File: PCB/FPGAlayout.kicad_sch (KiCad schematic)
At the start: 6 parts, among them U3 XC7A100T-FTG256

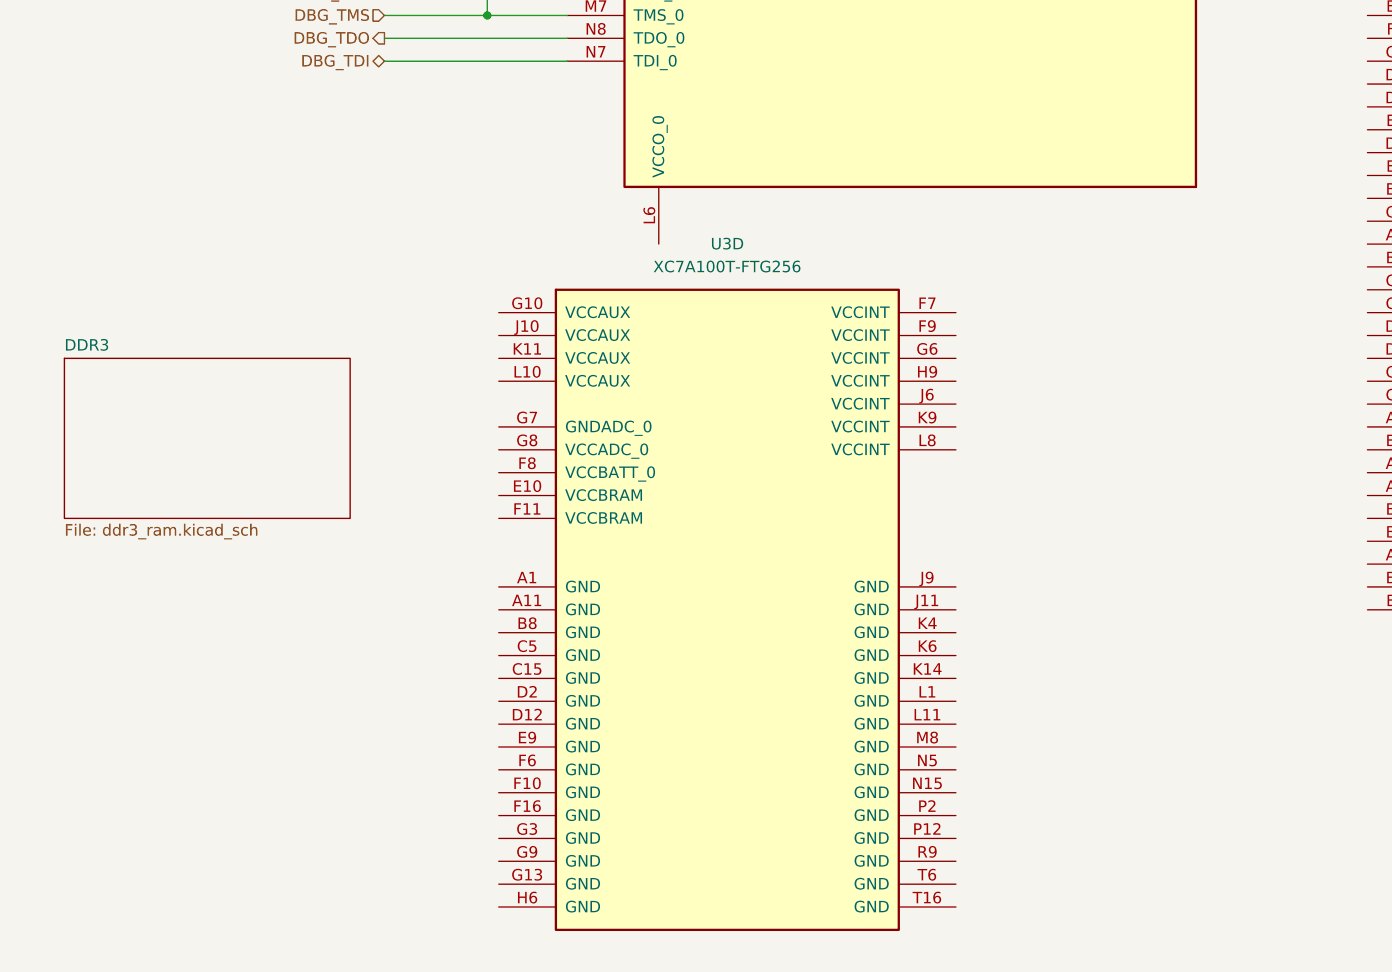
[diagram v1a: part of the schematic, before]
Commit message: Trace QSPI for MCU Master (#7), slaves unconnected
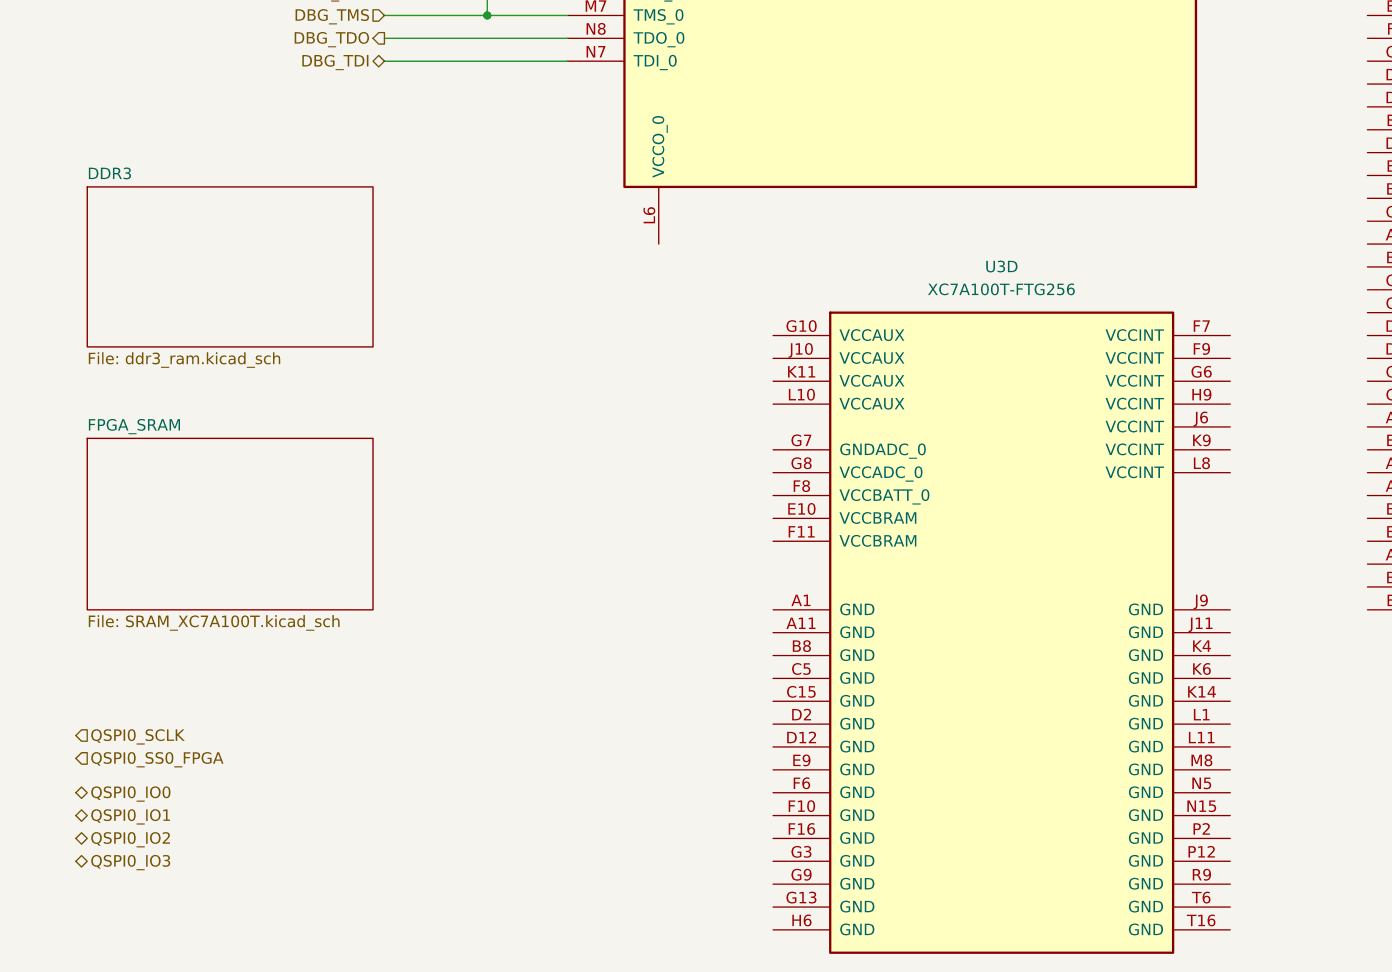
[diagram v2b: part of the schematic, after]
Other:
- added sheet FPGA_SRAM (SRAM_XC7A100T.kicad_sch)
- moved on the sheet: U3D
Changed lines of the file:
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@@
     (stroke (width 0) (type default))
+  )
+  (hierarchical_label "QSPI0_IO1" (shape bidirectional) (at 22.86 170.18 0) (fields_autoplaced)
+    (effects (font (size 1.27 1.27)) (justify left))
+  )
+  (hierarchical_label "QSPI0_SS0_FPGA" (shape input) (at 22.86 163.83 0) (fields_autoplaced)
+    (effects (font (size 1.27 1.27)) (justify left))
   )
   (hierarchical_label "PROGRAM_B_0" (shape output) (at 62.23 55.88 180) (fields_autoplaced)
@@
     (effects (font (size 1.27 1.27)) (justify right))
   )
+  (hierarchical_label "QSPI0_SCLK" (shape input) (at 22.86 161.29 0) (fields_autoplaced)
+    (effects (font (size 1.27 1.27)) (justify left))
+  )
+  (hierarchical_label "QSPI0_IO2" (shape bidirectional) (at 22.86 172.72 0) (fields_autoplaced)
+    (effects (font (size 1.27 1.27)) (justify left))
+  )
   (hierarchical_label "DBG_TMS" (shape input) (at 57.15 81.28 180) (fields_autoplaced)
     (effects (font (size 1.27 1.27)) (justify right))
   )
+  (hierarchical_label "QSPI0_IO0" (shape bidirectional) (at 22.86 167.64 0) (fields_autoplaced)
+    (effects (font (size 1.27 1.27)) (justify left))
+  )
   (hierarchical_label "DBG_TCK" (shape input) (at 57.15 78.74 180) (fields_autoplaced)
     (effects (font (size 1.27 1.27)) (justify right))
@@
   (hierarchical_label "DBG_TDI" (shape bidirectional) (at 57.15 86.36 180) (fields_autoplaced)
     (effects (font (size 1.27 1.27)) (justify right))
+  )
+  (hierarchical_label "QSPI0_IO3" (shape bidirectional) (at 22.86 175.26 0) (fields_autoplaced)
+    (effects (font (size 1.27 1.27)) (justify left))
   )
   (hierarchical_label "DBG_TDO" (shape output) (at 57.15 83.82 180) (fields_autoplaced)
@@
     )
   )
-  (symbol (lib_id "FPGA_Xilinx_Artix7:XC7A100T-FTG256") (at 95.25 147.32 0) (unit 4)
+  (symbol (lib_id "FPGA_Xilinx_Artix7:XC7A100T-FTG256") (at 125.73 149.86 0) (unit 4)
     (in_bom yes) (on_board yes) (dnp no) (fields_autoplaced)
-    (property "Reference" "U3" (at 95.25 106.68 0)
+    (property "Reference" "U3" (at 125.73 109.22 0)
       (effects (font (size 1.27 1.27)))
     )
-    (property "Value" "XC7A100T-FTG256" (at 95.25 109.22 0)
+    (property "Value" "XC7A100T-FTG256" (at 125.73 111.76 0)
       (effects (font (size 1.27 1.27)))
     )
-    (property "Footprint" "" (at 95.25 147.32 0)
-      (effects (font (size 1.27 1.27)) hide)
-    )
-    (property "Datasheet" "" (at 95.25 147.32 0)
+    (property "Footprint" "" (at 125.73 149.86 0)
+      (effects (font (size 1.27 1.27)) hide)
+    )
+    (property "Datasheet" "" (at 125.73 149.86 0)
       (effects (font (size 1.27 1.27)))
     )
@@
     )
   )
-  (sheet (at 21.59 119.38) (size 31.75 17.78) (fields_autoplaced)
+  (sheet (at 24.13 128.27) (size 31.75 19.05) (fields_autoplaced)
     (stroke (width 0.1524) (type solid))
     (fill (color 0 0 0 0.0000))
-    (property "Sheetname" "DDR3" (at 21.59 118.6684 0)
+    (property "Sheetname" "FPGA_SRAM" (at 24.13 127.5584 0)
       (effects (font (size 1.27 1.27)) (justify left bottom))
     )
-    (property "Sheetfile" "ddr3_ram.kicad_sch" (at 21.59 137.7446 0)
+    (property "Sheetfile" "SRAM_XC7A100T.kicad_sch" (at 24.13 147.9046 0)
       (effects (font (size 1.27 1.27)) (justify left top))
     )
+    (instances
+      (project "RayTracingPCB"
+        (path "/e9047d94-28be-4266-894b-6ee25ef088bd/5a7a2c0a-f09d-4b4f-9411-f51dd121457c" (page "10"))
+      )
+    )
+  )
+  (sheet (at 24.13 100.33) (size 31.75 17.78) (fields_autoplaced)
+    (stroke (width 0.1524) (type solid))
+    (fill (color 0 0 0 0.0000))
+    (property "Sheetname" "DDR3" (at 24.13 99.6184 0)
+      (effects (font (size 1.27 1.27)) (justify left bottom))
+    )
+    (property "Sheetfile" "ddr3_ram.kicad_sch" (at 24.13 118.6946 0)
+      (effects (font (size 1.27 1.27)) (justify left top))
+    )

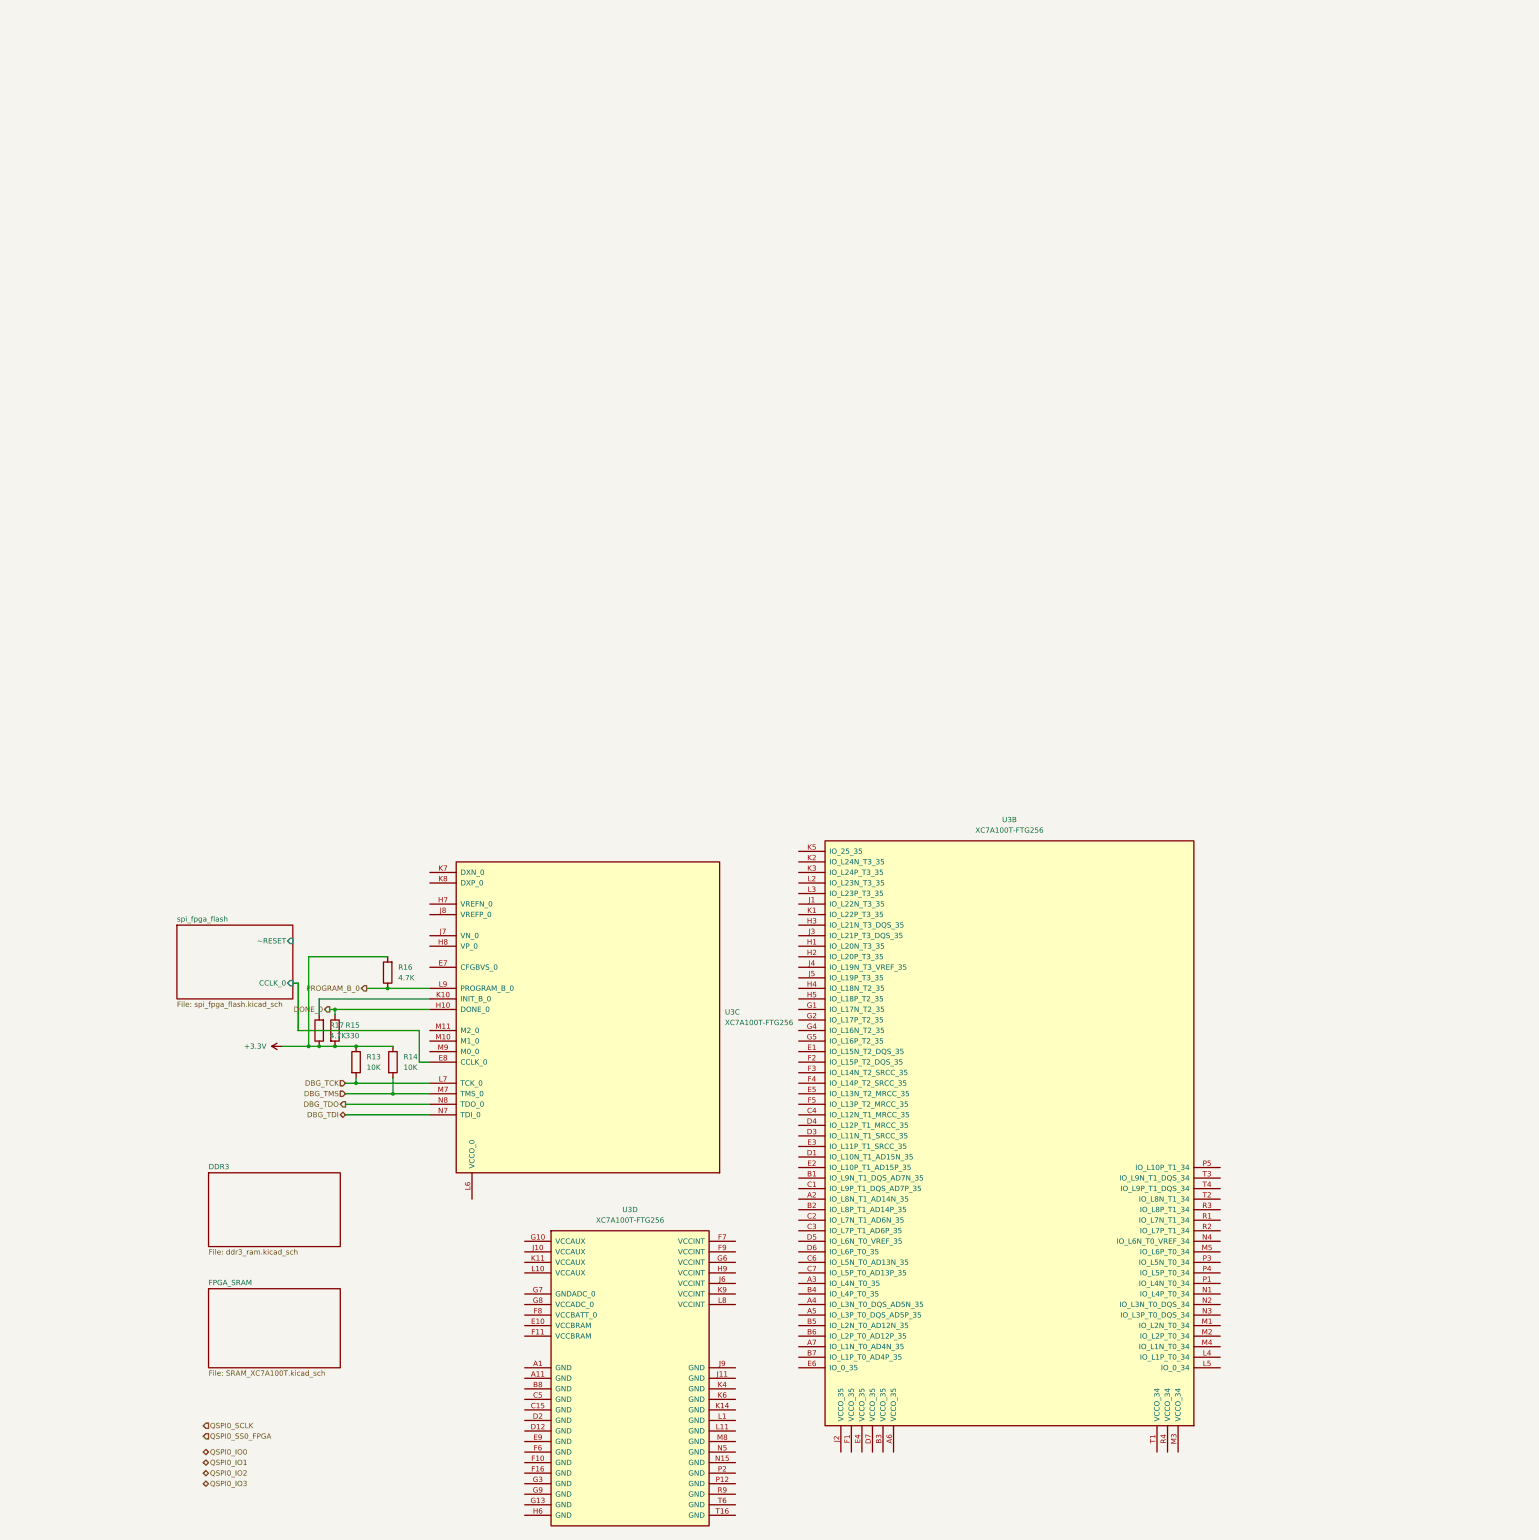
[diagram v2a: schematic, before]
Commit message: pcb: cleanup mcu sram (#10)
Co-authored-by: Kolbjørn Austreng <kolbjorn.austreng@hotzen.io>
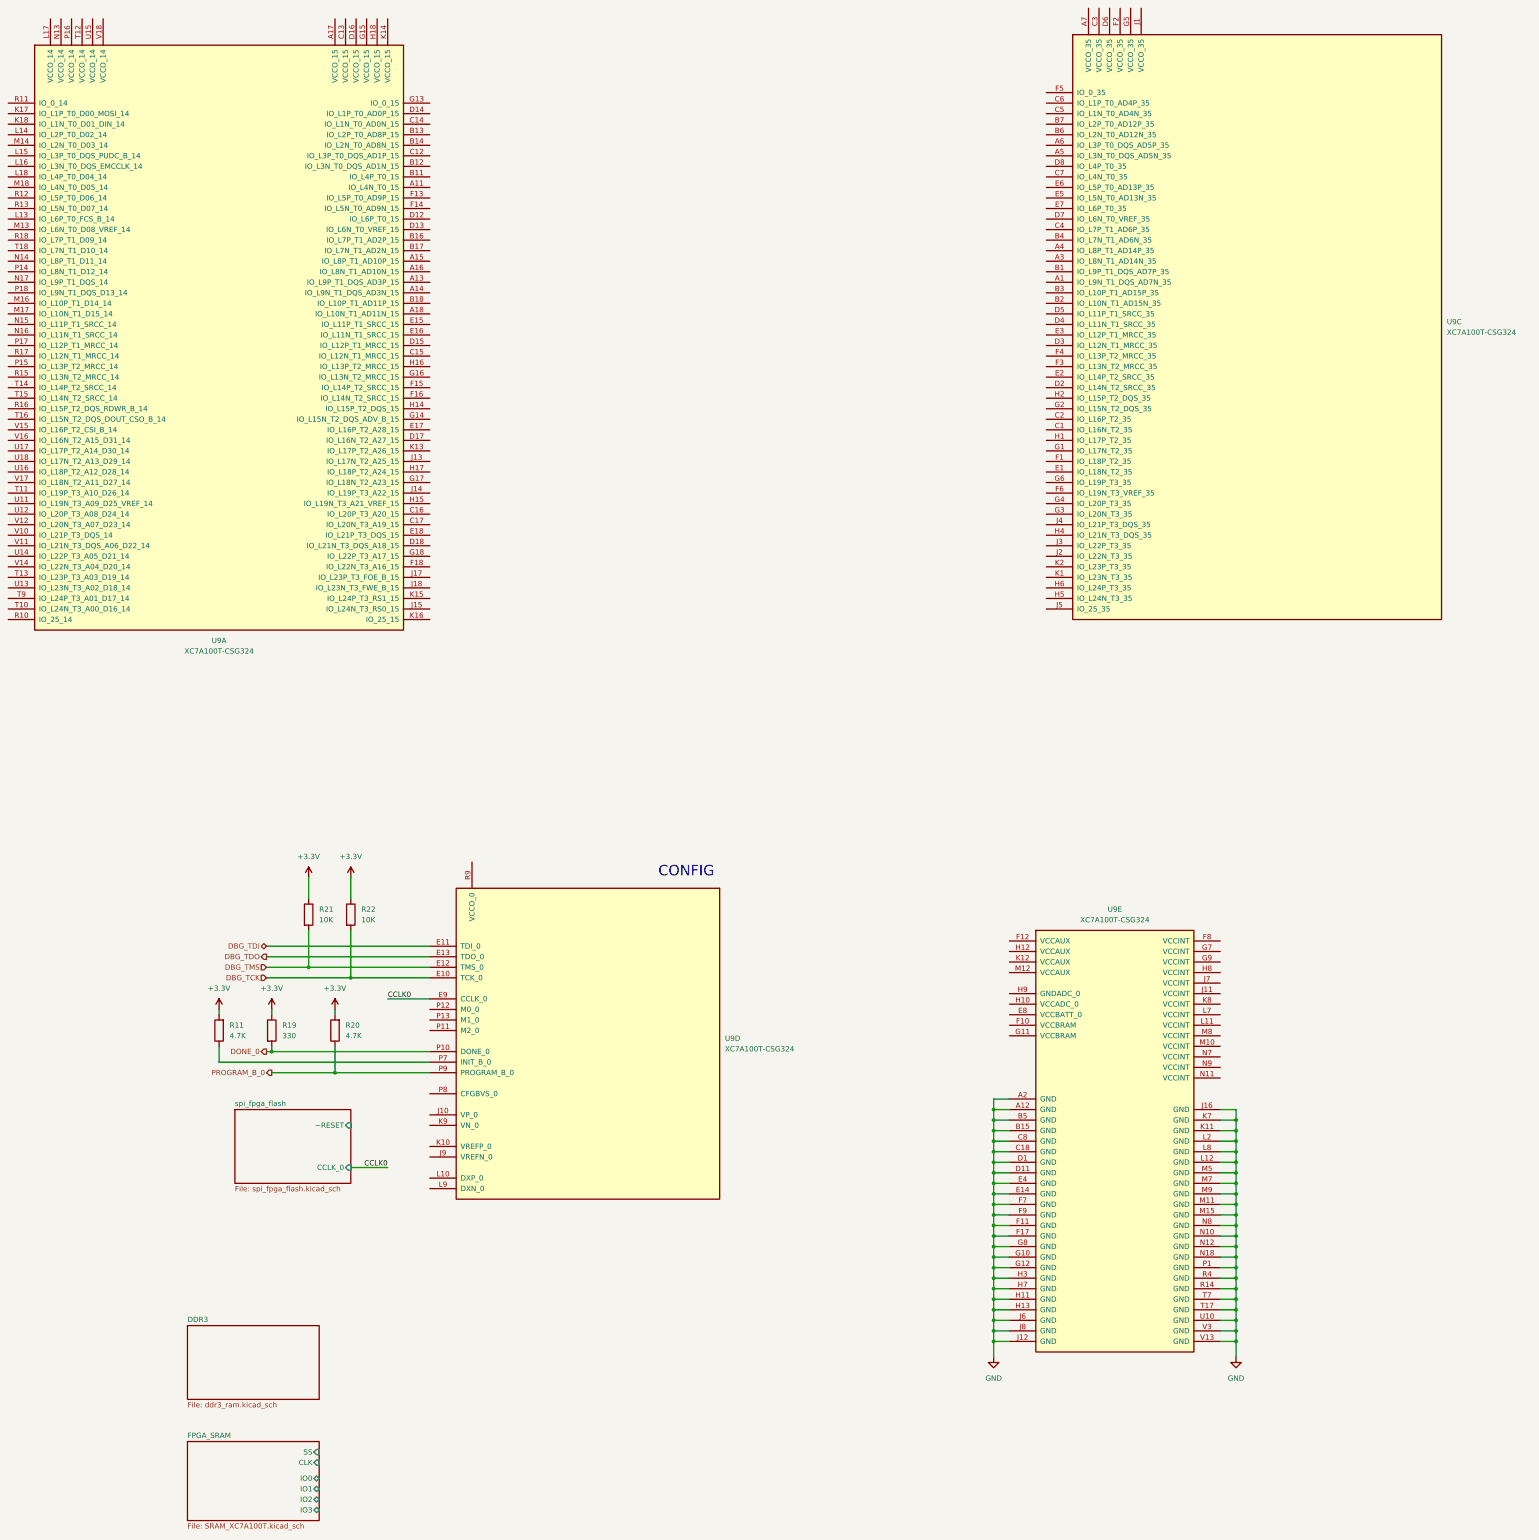
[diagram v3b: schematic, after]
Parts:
- removed R13, R14: 10K, symbol Device:R
- removed R15: 330, symbol Device:R
- removed R16, R17: 4.7K, symbol Device:R
- removed U3: XC7A100T-FTG256, symbol FPGA_Xilinx_Artix7:XC7A100T-FTG256
- added R11, R20: 4.7K, symbol Device:R
- added R19: 330, symbol Device:R
- added R21, R22: 10K, symbol Device:R
- added U9: XC7A100T-CSG324, symbol FPGA_Xilinx_Artix7:XC7A100T-CSG324
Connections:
- net +3.3V: now also R11.2, R19.1, R20.2, R21.1, R22.1
- net DBG_TCK: now also R22.2, U9.E10 (TCK_0)
- net DBG_TDI: now also U9.E11 (TDI_0)
- net DBG_TDO: now also U9.E13 (TDO_0)
- net DBG_TMS: now also R21.2, U9.E12 (TMS_0)
- net DONE_0: now also R19.2, U9.P10 (DONE_0)
- net PROGRAM_B_0: now also R20.1, U9.P9 (PROGRAM_B_0)
- new net: R11.1, U9.P7 (INIT_B_0)
- new net CCLK0: U9.E9 (CCLK_0)
- new net GND: U9.A12 (GND), U9.A2 (GND), U9.B15 (GND), U9.B5 (GND), U9.C18 (GND), U9.C8 (GND), U9.D1 (GND), U9.D11 (GND), U9.E14 (GND), U9.E4 (GND), U9.F11 (GND), U9.F17 (GND), U9.F7 (GND), U9.F9 (GND), U9.G10 (GND), U9.G12 (GND), U9.G8 (GND), U9.H11 (GND), U9.H13 (GND), U9.H3 (GND), U9.H7 (GND), U9.J12 (GND), U9.J16 (GND), U9.J6 (GND), U9.J8 (GND), U9.K11 (GND), U9.K7 (GND), U9.L12 (GND), U9.L2 (GND), U9.L8 (GND), U9.M11 (GND), U9.M15 (GND), U9.M5 (GND), U9.M7 (GND), U9.M9 (GND), U9.N10 (GND), U9.N12 (GND), U9.N18 (GND), U9.N8 (GND), U9.P1 (GND), U9.R14 (GND), U9.R4 (GND), U9.T17 (GND), U9.T7 (GND), U9.U10 (GND), U9.V13 (GND), U9.V3 (GND)
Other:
- sheet FPGA_SRAM ports: added CLK, IO0, IO1, IO2, IO3, SS; removed none
- note added: "CONFIG"

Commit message: dump
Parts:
- removed unit 3 of U9
- removed unit 1 of U9
- added C34, C35, C40, C45, C46, C47, C52, C53, C54: 4.7u, symbol Device:C_Small
- added C36: 100u, symbol Device:C_Polarized_Small_US
- added C37, C38, C41, C42, C43, C44, C48, C49, C50, C51: 470n, symbol Device:C_Small
- added C39, C55: 47u, symbol Device:C_Small
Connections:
- net +3.3V: now also U9.P12 (M0_0), U9.R9 (VCCO_0), C41.1, C42.1, C43.1, C44.1, C45.1, C46.1, C47.1, C48.1, C49.1, C50.1, C51.1, C52.1, C53.1, C54.1, C55.1
- net GND: now also U9.E8 (VCCBATT_0), U9.H10 (VCCADC_0), U9.H9 (GNDADC_0), U9.J10 (VP_0), U9.J9 (VREFN_0), U9.K10 (VREFP_0), U9.K9 (VN_0), U9.P11 (M2_0), U9.P13 (M1_0), U9.P8 (CFGBVS_0), C34.2, C35.2, C36.2, C37.2, C38.2, C39.2, C40.2, C41.2, C42.2, C43.2, C44.2, C45.2, C46.2, C47.2, C48.2, C49.2, C50.2, C51.2, C52.2, C53.2, C54.2, C55.2
- net +1V0: now reaches U9.F10 (VCCBRAM)
- net +1V0: now also U9.F8 (VCCINT), U9.G11 (VCCBRAM), U9.G7 (VCCINT), U9.G9 (VCCINT), U9.H8 (VCCINT), U9.J11 (VCCINT), U9.J7 (VCCINT), U9.K8 (VCCINT), U9.L11 (VCCINT), U9.L7 (VCCINT), U9.M10 (VCCINT), U9.M8 (VCCINT), U9.N11 (VCCINT), U9.N7 (VCCINT), U9.N9 (VCCINT), C34.1, C35.1, C36.1, C37.1, C38.1
- net +1V8: now reaches U9.F12 (VCCAUX)
- net +1V8: now also U9.H12 (VCCAUX), U9.K12 (VCCAUX), U9.M12 (VCCAUX), C39.1, C40.1
- no-connect marks 0 -> 2
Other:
- added sheet FPGA_IO_CD (untitled.kicad_sch)
- note added: "Vcc0"
- note added: "Vccbram"
- note added: "Vccint"
- moved on the sheet: U9E
